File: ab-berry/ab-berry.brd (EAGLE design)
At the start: 58.4 x 61 mm, 64 parts, among them U1 LM1117MPX-3.3/NOPB or AP2114H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

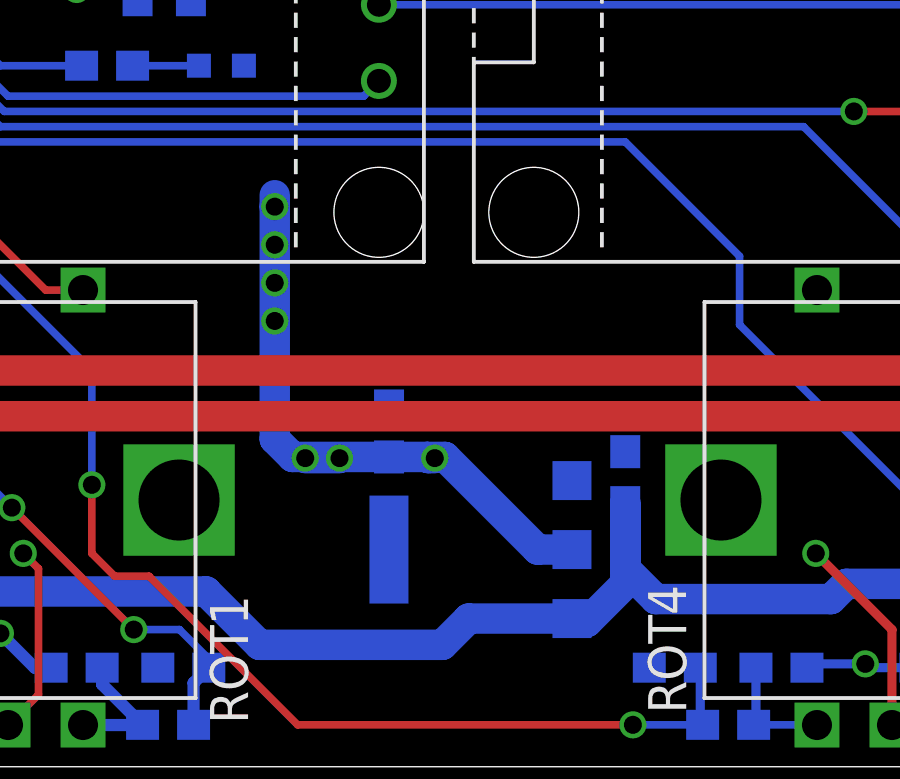
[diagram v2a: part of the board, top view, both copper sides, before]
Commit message: ab-berry: switch tantalum caps footprint
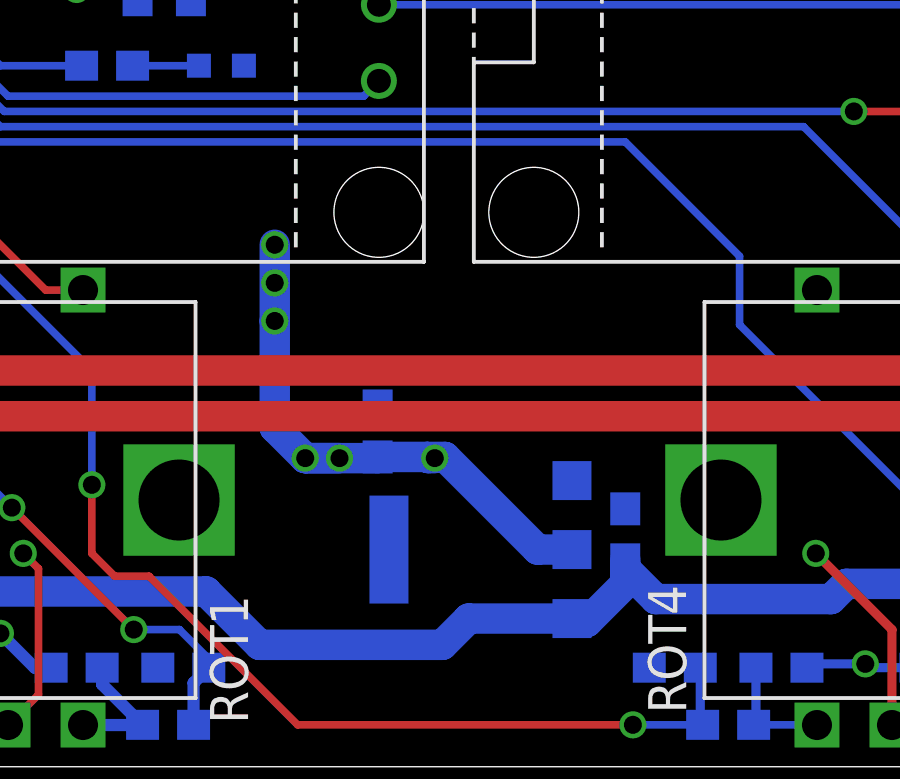
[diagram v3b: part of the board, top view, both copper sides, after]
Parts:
- C8, C9: value 10uF Tantalum -> 10uF TANT; device microbuilder:0603 -> SparkFun-Capacitors:0603-POL
- moved C8 1.90 mm to (35.1, 7.75)
- moved C9 0.38 mm to (26.8, 11.2), turned to 270 degrees
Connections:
- net 3.3V: now also C9.A; no longer C9.1
- net 5.0V: now also C8.A; no longer C8.2
- net GND: now also C8.K, C9.K; no longer C8.1, C9.2
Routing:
- net 5.0V: track 64.8 -> 60.7 mm
- net 3.3V: track 75.6 -> 73.8 mm, vias 20 -> 19
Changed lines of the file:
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@@
 <layer number="54" name="bGND_GNDA" color="1" fill="9" visible="no" active="no"/>
 <layer number="56" name="wert" color="7" fill="1" visible="yes" active="yes"/>
+<layer number="57" name="tCAD" color="7" fill="1" visible="no" active="no"/>
 <layer number="90" name="Modules" color="5" fill="1" visible="no" active="no"/>
 <layer number="91" name="Nets" color="2" fill="1" visible="no" active="no"/>
@@
 <layer number="97" name="Info" color="7" fill="1" visible="no" active="no"/>
 <layer number="98" name="Guide" color="6" fill="1" visible="no" active="no"/>
+<layer number="99" name="SpiceOrder" color="7" fill="1" visible="no" active="no"/>
 <layer number="100" name="Muster" color="7" fill="1" visible="yes" active="yes"/>
 <layer number="101" name="Patch_Top" color="12" fill="4" visible="yes" active="yes"/>
@@
 <layer number="111" name="MPL" color="7" fill="1" visible="yes" active="yes"/>
 <layer number="112" name="tSilk" color="7" fill="1" visible="yes" active="yes"/>
+<layer number="113" name="IDFDebug" color="7" fill="1" visible="yes" active="yes"/>
 <layer number="116" name="Patch_BOT" color="9" fill="4" visible="yes" active="yes"/>
 <layer number="121" name="sName" color="7" fill="1" visible="yes" active="yes"/>
@@
 <layer number="132" name="bAdjust" color="7" fill="1" visible="no" active="yes"/>
 <layer number="144" name="Drill_legend" color="7" fill="1" visible="yes" active="yes"/>
+<layer number="150" name="Notes" color="7" fill="1" visible="yes" active="yes"/>
 <layer number="151" name="HeatSink" color="7" fill="1" visible="yes" active="yes"/>
 <layer number="152" name="_bDocu" color="7" fill="1" visible="yes" active="yes"/>
+<layer number="153" name="FabDoc1" color="7" fill="1" visible="yes" active="yes"/>
+<layer number="154" name="FabDoc2" color="7" fill="1" visible="yes" active="yes"/>
+<layer number="155" name="FabDoc3" color="7" fill="1" visible="yes" active="yes"/>
 <layer number="199" name="Contour" color="7" fill="1" visible="yes" active="yes"/>
 <layer number="200" name="200bmp" color="1" fill="10" visible="yes" active="yes"/>
@@
 <layer number="223" name="223bmp" color="24" fill="1" visible="no" active="no"/>
 <layer number="224" name="224bmp" color="25" fill="1" visible="no" active="no"/>
+<layer number="225" name="225bmp" color="7" fill="1" visible="yes" active="yes"/>
+<layer number="226" name="226bmp" color="7" fill="1" visible="yes" active="yes"/>
+<layer number="227" name="227bmp" color="7" fill="1" visible="yes" active="yes"/>
+<layer number="228" name="228bmp" color="7" fill="1" visible="yes" active="yes"/>
+<layer number="229" name="229bmp" color="7" fill="1" visible="yes" active="yes"/>
+<layer number="230" name="230bmp" color="7" fill="1" visible="yes" active="yes"/>
 <layer number="231" name="Eagle3D_PG1" color="14" fill="1" visible="yes" active="yes"/>
 <layer number="232" name="Eagle3D_PG2" color="14" fill="2" visible="yes" active="yes"/>
@@
 <layer number="251" name="SMDround" color="7" fill="1" visible="yes" active="yes"/>
 <layer number="254" name="cooling" color="7" fill="1" visible="yes" active="yes"/>
+<layer number="255" name="routoute" color="7" fill="1" visible="yes" active="yes"/>
 </layers>
 <board>
@@
 <attribute name="NAME" x="30.099" y="10.033" size="0.8128" layer="26" ratio="18" rot="MR270"/>
 </element>
-<element name="C8" library="microbuilder" package="0603" value="10uF Tantalum" x="35.052" y="9.652" smashed="yes" rot="MR270">
-<attribute name="NAME" x="34.417" y="12.192" size="0.8128" layer="26" font="vector" ratio="18" rot="MR180"/>
-<attribute name="VALUE" x="36.322" y="11.684" size="0.4064" layer="28" font="vector" ratio="10" rot="MR270"/>
-</element>
-<element name="C9" library="microbuilder" package="0603" value="10uF Tantalum" x="27.178" y="11.176" smashed="yes" rot="MR90">
-<attribute name="NAME" x="27.051" y="12.954" size="0.8128" layer="26" font="vector" ratio="18" rot="MR90"/>
-<attribute name="VALUE" x="25.908" y="9.398" size="0.4064" layer="28" font="vector" ratio="10" rot="MR90"/>
-</element>
 <element name="LED1" library="microbuilder" package="CHIPLED_0603" value="" x="25.527" y="51.816" rot="MR180"/>
 <element name="R5" library="microbuilder" package="0603" value="330" x="25.527" y="55.372" rot="MR90"/>
@@
 <element name="R22" library="microbuilder" package="0603" value="10K" x="47.244" y="48.768" smashed="yes" rot="MR0">
 <attribute name="NAME" x="46.228" y="49.657" size="0.8128" layer="26" font="vector" ratio="18" rot="MR0"/>
+</element>
+<element name="C8" library="SparkFun-Capacitors" package="0603-POL" value="10uF TANT" x="35.052" y="7.747" smashed="yes" rot="MR270">
+<attribute name="PROD_ID" value="CAP-13210" x="35.052" y="7.747" size="1.778" layer="28" rot="MR270" display="off"/>
+<attribute name="NAME" x="34.29" y="8.636" size="0.4064" layer="26" font="vector" rot="MR270"/>
+<attribute name="VALUE" x="35.814" y="6.858" size="0.4064" layer="28" font="vector" rot="MR90"/>
+</element>
+<element name="C9" library="SparkFun-Capacitors" package="0603-POL" value="10uF TANT" x="26.797" y="11.176" smashed="yes" rot="MR270">
+<attribute name="PROD_ID" value="CAP-13210" x="26.797" y="11.176" size="1.778" layer="28" rot="MR270" display="off"/>
+<attribute name="NAME" x="26.035" y="12.065" size="0.4064" layer="26" font="vector" rot="MR270"/>
+<attribute name="VALUE" x="28.067" y="13.081" size="0.4064" layer="28" font="vector" rot="MR270"/>
 </element>
 </elements>
@@
 <contactref element="R2" pad="2"/>
 <contactref element="C7" pad="2"/>
-<contactref element="C8" pad="1"/>
 <contactref element="LED1" pad="C"/>
-<contactref element="C9" pad="2"/>
 <contactref element="U1" pad="1"/>
 <contactref element="ROT1" pad="C"/>
@@
 <contactref element="C20" pad="2"/>
 <contactref element="C21" pad="2"/>
+<contactref element="C8" pad="K"/>
+<contactref element="C9" pad="K"/>
 </signal>
 <signal name="3.3V">
@@
 <contactref element="U1" pad="2"/>
 <contactref element="R5" pad="2"/>
-<contactref element="C9" pad="1"/>
 <contactref element="LCD1" pad="VCC"/>
 <contactref element="C10" pad="1"/>
@@
 <vertex x="-1.905" y="-3.81"/>
 </polygon>
-<wire x1="27.178" y1="10.326" x2="28.448" y2="10.326" width="1.016" layer="16"/>
 <wire x1="28.448" y1="10.326" x2="29.044" y2="10.326" width="1.016" layer="16"/>
 <wire x1="29.044" y1="10.326" x2="32.131" y2="7.239" width="1.016" layer="16"/>
 <wire x1="32.131" y1="7.239" x2="33.276" y2="7.239" width="1.016" layer="16"/>
-<wire x1="27.178" y1="10.326" x2="23.964" y2="10.326" width="1.016" layer="16"/>
 <via x="28.702" y="10.287" extent="1-16" drill="0.6"/>
 <via x="25.527" y="10.287" extent="1-16" drill="0.6"/>
@@
 <via x="1.778" y="45.974" extent="1-16" drill="0.6"/>
 <wire x1="1.778" y1="45.974" x2="1.27" y2="45.466" width="0.254" layer="1"/>
-<wire x1="23.964" y1="10.326" x2="23.368" y2="10.922" width="1.016" layer="16"/>
-<wire x1="23.368" y1="10.922" x2="23.368" y2="18.669" width="1.016" layer="16"/>
 <via x="23.368" y="14.859" extent="1-16" drill="0.6"/>
 <via x="23.368" y="16.129" extent="1-16" drill="0.6"/>
 <via x="23.368" y="17.399" extent="1-16" drill="0.6"/>
-<via x="23.368" y="18.669" extent="1-16" drill="0.6"/>
-<wire x1="23.368" y1="18.669" x2="23.368" y2="19.05" width="1.016" layer="16"/>
 <wire x1="17.358" y1="30.119" x2="18.649" y2="30.119" width="0.254" layer="16"/>
 <wire x1="18.649" y1="30.119" x2="18.796" y2="29.972" width="0.254" layer="16"/>
@@
 <via x="47.244" y="50.038" extent="1-16" drill="0.6"/>
 <wire x1="47.244" y1="50.038" x2="46.99" y2="50.292" width="0.254" layer="1"/>
+<contactref element="C9" pad="A"/>
+<wire x1="28.448" y1="10.326" x2="26.797" y2="10.326" width="1.016" layer="16"/>
+<wire x1="24.384" y1="10.287" x2="26.797" y2="10.287" width="1.016" layer="16"/>
+<wire x1="26.797" y1="10.287" x2="26.797" y2="10.326" width="1.016" layer="16"/>
+<wire x1="23.368" y1="14.859" x2="23.368" y2="17.399" width="1.016" layer="16"/>
+<wire x1="24.384" y1="10.287" x2="23.368" y2="11.303" width="1.016" layer="16"/>
+<wire x1="23.368" y1="11.303" x2="23.368" y2="14.859" width="1.016" layer="16"/>
 </signal>
 <signal name="SWDIO">
@@
 <signal name="5.0V">
 <contactref element="U1" pad="3"/>
-<contactref element="C8" pad="2"/>
 <contactref element="JP1" pad="1"/>
 <contactref element="JP2" pad="1"/>
@@
 <wire x1="21.082" y1="5.842" x2="22.86" y2="4.064" width="1.016" layer="16"/>
 <wire x1="22.86" y1="4.064" x2="28.956" y2="4.064" width="1.016" layer="16"/>
-<wire x1="35.052" y1="8.802" x2="35.052" y2="6.096" width="1.016" layer="16"/>
 <wire x1="35.052" y1="6.096" x2="33.782" y2="4.826" width="1.016" layer="16"/>
 <wire x1="33.782" y1="4.826" x2="33.389" y2="4.826" width="1.016" layer="16"/>
 <wire x1="33.389" y1="4.826" x2="33.276" y2="4.939" width="1.016" layer="16"/>
-<wire x1="35.052" y1="8.802" x2="35.052" y2="6.604" width="1.016" layer="16"/>
 <wire x1="35.052" y1="6.604" x2="36.068" y2="5.588" width="1.016" layer="16"/>
 <wire x1="36.068" y1="5.588" x2="41.91" y2="5.588" width="1.016" layer="16"/>
@@
 <wire x1="54.356" y1="7.62" x2="56.769" y2="7.62" width="1.016" layer="16"/>
 <wire x1="56.769" y1="7.62" x2="57.15" y2="8.001" width="1.016" layer="16"/>
+<contactref element="C8" pad="A"/>
+<wire x1="35.052" y1="6.604" x2="35.052" y2="6.096" width="1.016" layer="16"/>
+<wire x1="35.052" y1="6.604" x2="35.052" y2="6.897" width="1.016" layer="16"/>
 </signal>
 <signal name="ROT1_A">
